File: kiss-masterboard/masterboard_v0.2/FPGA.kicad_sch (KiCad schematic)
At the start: 89 parts, among them J10 CRESET, J11 Jumper, J12 Jumper, J13 Conn_02x08_Odd_Even, J14 Conn_02x08_Odd_Even, J15 jmp, J16 jmp, J8 Jumper, U11 TLV75733PDBV, U13 SN74LVC8T245, U14 W25Q, U17 12MHz, U2 SN74LVC8T245, U4 ICE40UP5k-SG48, U5 SN74LVC8T245, U8 TLV75709PDBV

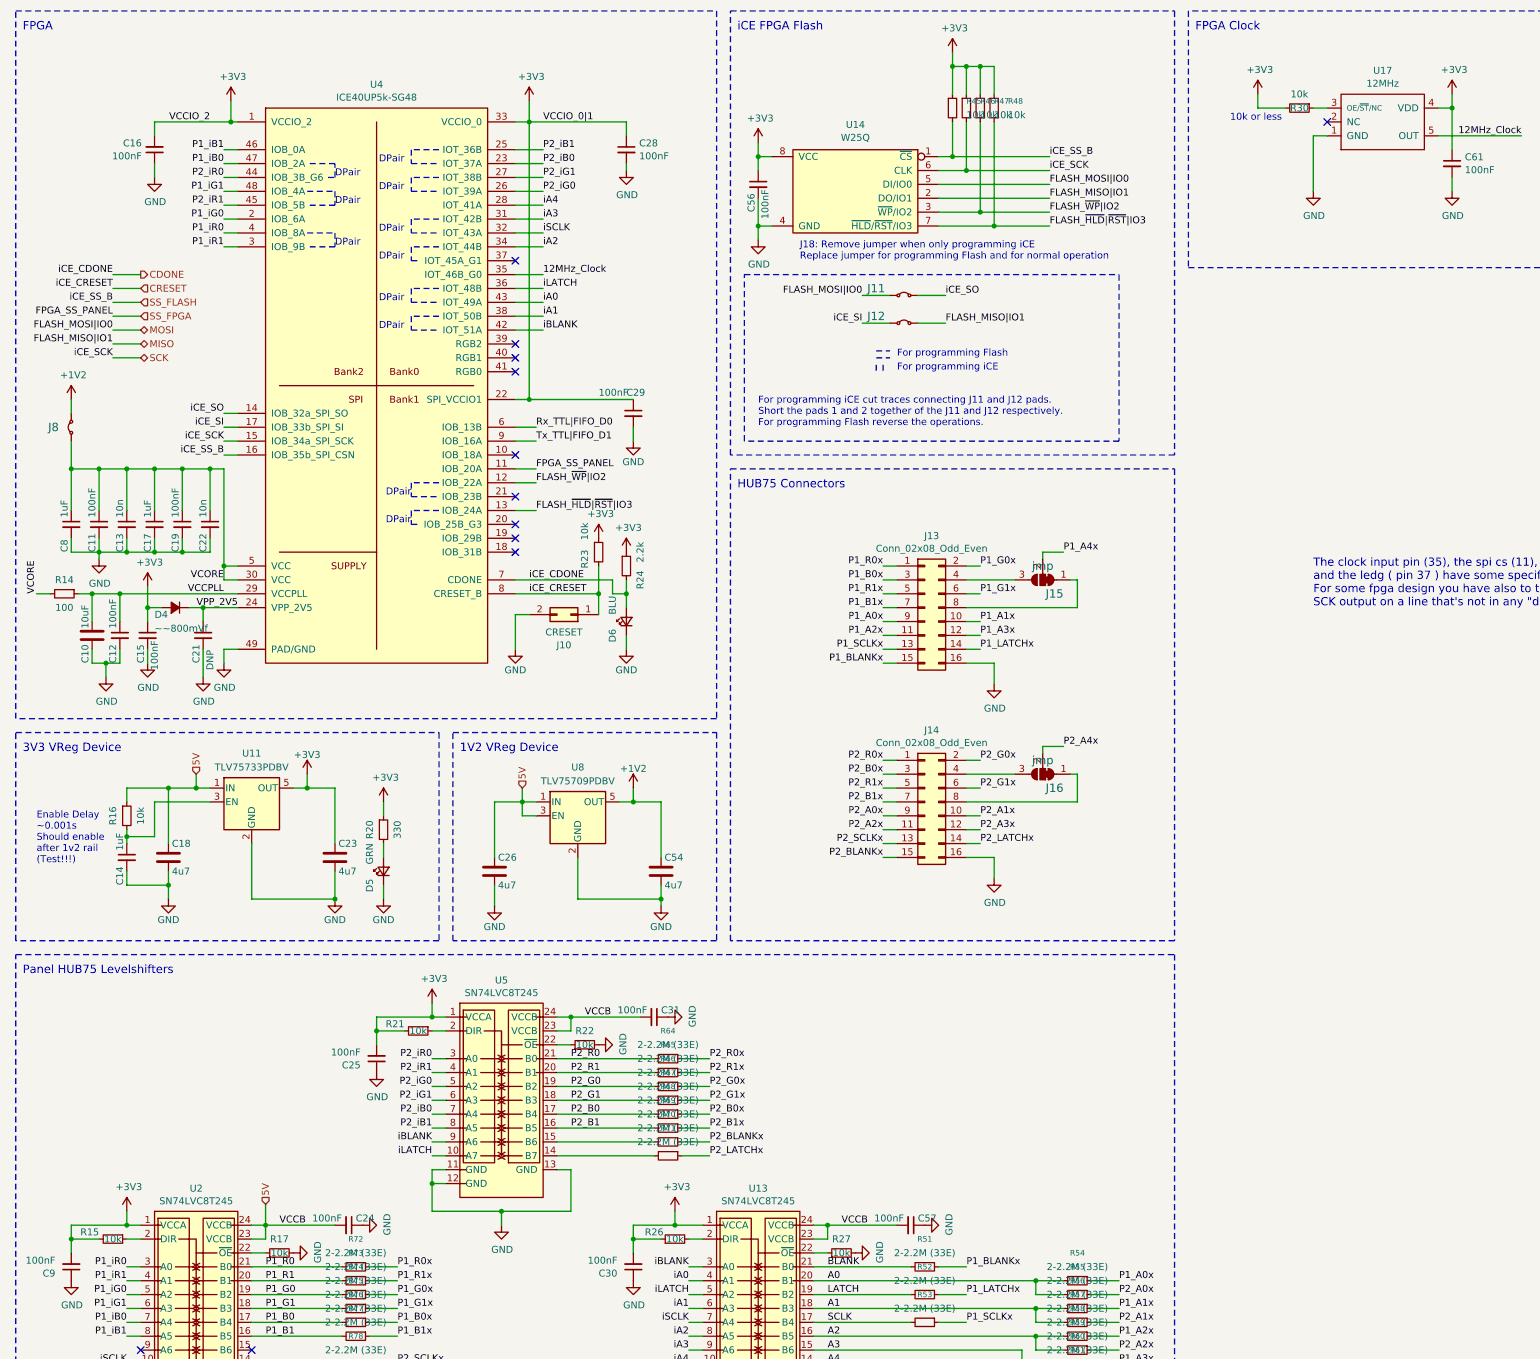
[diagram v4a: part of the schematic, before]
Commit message: add cnumbers initial order v04a
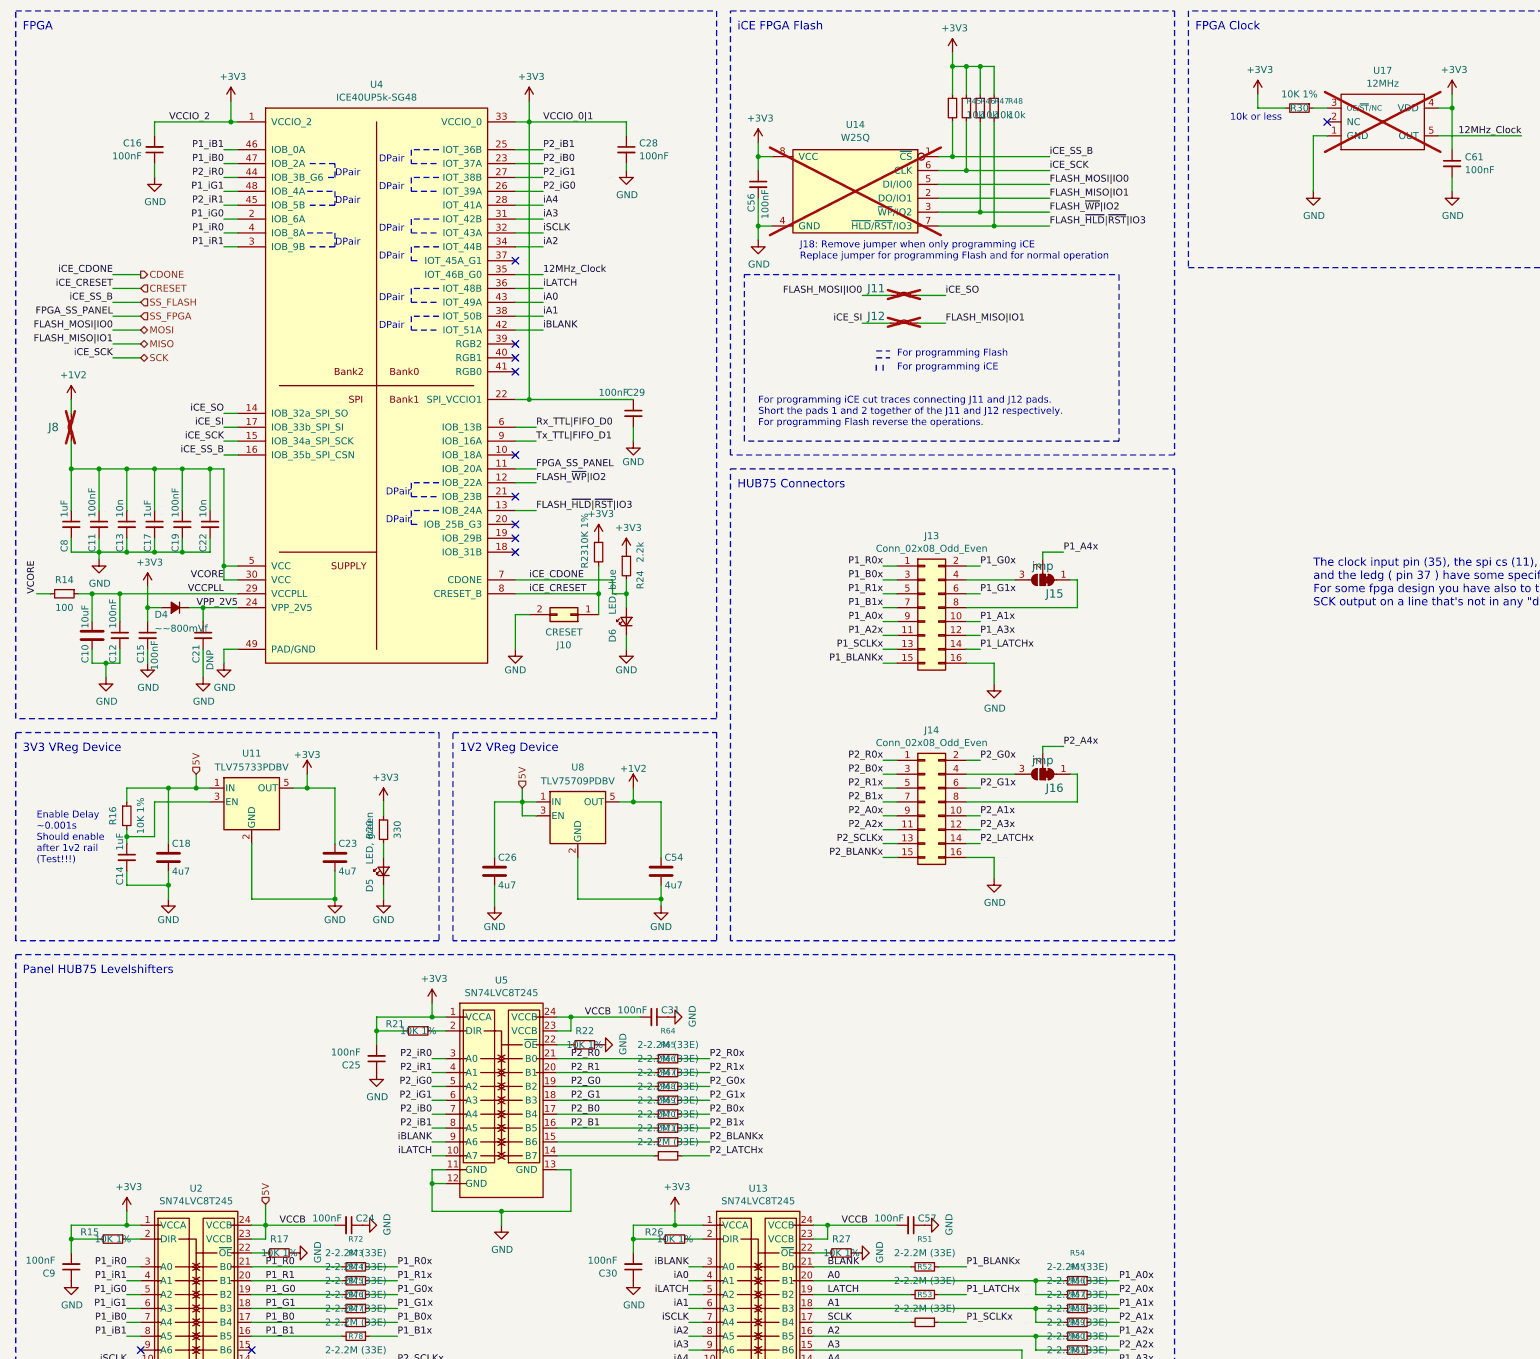
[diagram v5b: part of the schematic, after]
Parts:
- C10: JLCNR (none) -> C19702
- C11, C12, C15, C16, C19, C24, C25, C28, C29, C30, C31, C57, C61, C9: JLCNR (none) -> C1525
- C13, C22: JLCNR (none) -> C15195
- C14, C17, C8: JLCNR (none) -> C52923
- C18, C23, C26, C54: JLCNR (none) -> C19666
- C56: JLCNR (none) -> C14663
- D4: JLCNR (none) -> C7502714
- D5: value GRN -> LED, green; JLCNR (none) -> C2290
- D6: value BLU -> LED, blue; JLCNR (none) -> C2286
- J11, J12, J8, U14, U17: now not fitted
- J13, J14: JLCNR (none) -> C32713288
- R14: JLCNR (none) -> C25076
- R15, R16, R17, R21, R22, R23, R26, R27, R30: value 10k -> 10K 1%; JLCNR (none) -> C25744
- R20: JLCNR (none) -> C25104
- R24: JLCNR (none) -> C25879
- R45, R46, R47, R48: JLCNR (none) -> C25804
- R51, R52, R53, R54, R55, R56, R57, R58, R59, R60, R61, R62, R63, R64, R65, R66, R67, R68, R69, R70, R71, R72, R73, R74, R75, R76, R77, R78: JLCNR (none) -> C138015
- U11: JLCNR (none) -> C485517
- U13, U2, U5: JLCNR (none) -> C27643
- U4: JLCNR (none) -> C2678152
- U8: JLCNR (none) -> C58464
